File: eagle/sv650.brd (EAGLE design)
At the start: 54.2 x 52 mm, 32 parts, among them Q1 IRLML6344

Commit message: reroute some traces to be cleaner ordered v4.6 via oshpark
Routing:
- net GND: track 161.4 -> 159.8 mm
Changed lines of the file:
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@@
 </element>
 <element name="JP3" library="jumper" package="JP2" value="" x="18.29" y="44.29" smashed="yes" rot="MR90">
-<attribute name="NAME" x="16.401" y="49.574" size="1.27" layer="26" ratio="10" rot="MR180"/>
+<attribute name="NAME" x="14.201" y="43.004" size="1.27" layer="26" ratio="10" rot="MR90"/>
 <attribute name="VALUE" x="13.972" y="40.734" size="1.27" layer="28" ratio="10" rot="MR90"/>
 </element>
@@
 <wire x1="9.1152" y1="16.128" x2="9.1152" y2="11.7152" width="0.3048" layer="1"/>
 <wire x1="9.1152" y1="11.7152" x2="8.38" y2="10.98" width="0.3048" layer="1"/>
-<wire x1="8.38" y1="10.98" x2="7.16" y2="10.98" width="0.3048" layer="1"/>
-<wire x1="7.16" y1="10.98" x2="6.1" y2="10.98" width="0.3048" layer="1"/>
-<wire x1="6.1" y1="10.98" x2="4.37" y2="12.71" width="0.3048" layer="1"/>
-<wire x1="4.37" y1="12.71" x2="4.37" y2="14.57" width="0.3048" layer="1"/>
-<wire x1="4.37" y1="14.57" x2="4.29" y2="14.65" width="0.3048" layer="1"/>
-<wire x1="7.16" y1="10.98" x2="7.16" y2="8.36" width="0.3048" layer="1"/>
+<wire x1="8.38" y1="10.98" x2="7.16" y2="9.85" width="0.3048" layer="1"/>
+<wire x1="7.16" y1="9.85" x2="7.16" y2="8.36" width="0.3048" layer="1"/>
 <wire x1="17.12" y1="19.61" x2="17.17" y2="19.61" width="0.3048" layer="16"/>
 <wire x1="17.17" y1="19.61" x2="17.17" y2="22.56" width="0.3048" layer="16"/>
@@
 <wire x1="4.75" y1="6.57" x2="4.75" y2="5.84" width="0.3048" layer="1"/>
 <wire x1="4.75" y1="5.84" x2="3.62" y2="4.71" width="0.3048" layer="1"/>
-<wire x1="5.12" y1="9.86" x2="5.66" y2="9.86" width="0.3048" layer="1"/>
-<wire x1="5.66" y1="9.86" x2="7.16" y2="8.36" width="0.3048" layer="1"/>
 <wire x1="16.36" y1="14.36" x2="16.36" y2="15.15" width="0.3048" layer="1"/>
 <wire x1="16.36" y1="15.15" x2="18.32" y2="17.11" width="0.3048" layer="1"/>
@@
 <wire x1="19.34" y1="43.26" x2="10.04" y2="43.26" width="0.3048" layer="1"/>
 <wire x1="10.04" y1="43.26" x2="9.275784375" y2="42.495784375" width="0.3048" layer="16"/>
+<wire x1="4.29" y1="14.65" x2="5.12" y2="13.82" width="0.3048" layer="1"/>
+<wire x1="5.12" y1="13.82" x2="5.12" y2="9.86" width="0.3048" layer="1"/>
+<wire x1="5.12" y1="9.86" x2="6.17" y2="9.85" width="0.3048" layer="1"/>
+<wire x1="6.17" y1="9.85" x2="7.16" y2="9.85" width="0.3048" layer="1"/>
 </signal>
 <signal name="N$2">

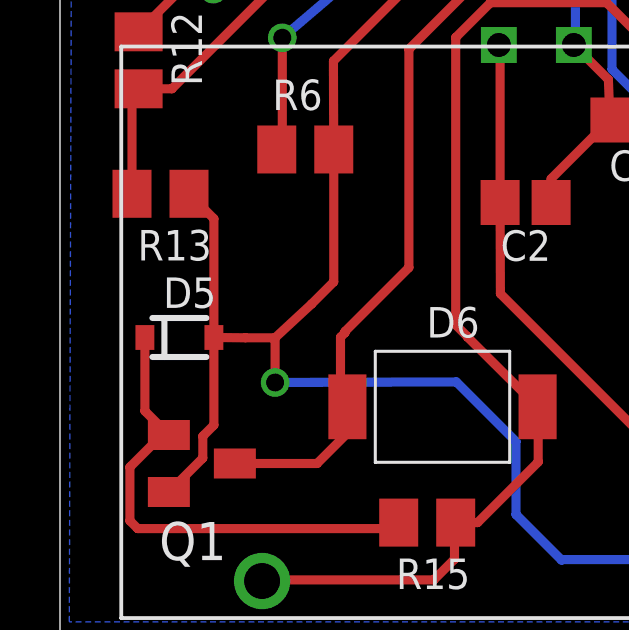
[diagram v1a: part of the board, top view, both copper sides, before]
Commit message: switch D5 to a SOD-123 package
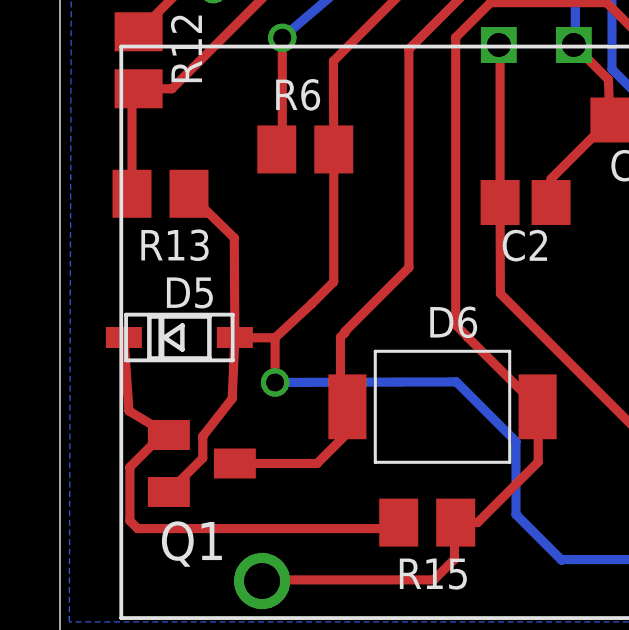
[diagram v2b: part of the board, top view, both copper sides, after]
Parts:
- D5: device SparkFun-DiscreteSemi:SOD-323 -> adafruit:SOD-123
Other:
- board text added: "20140907"
- board text added: "http://synfin.net/sv650ecu SV650 ECU Decoder v4.7"
- board text removed: "20140518"
- board text removed: "http://synfin.net/sv650ecu SV650 ECU Decoder v4.6"
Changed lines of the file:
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@@
 <?xml version="1.0" encoding="utf-8"?>
 <!DOCTYPE eagle SYSTEM "eagle.dtd">
-<eagle version="6.5.0">
+<eagle version="7.1.0">
 <drawing>
 <settings>
@@
 <hole x="50.546" y="29.464" drill="5.1562"/>
 <text x="40.548" y="48.252" size="1.27" layer="22" font="vector" rot="MR0">http://synfin.net/sv650ecu
-SV650 ECU Decoder v4.6</text>
+SV650 ECU Decoder v4.7</text>
 <text x="53.534" y="36.688" size="1.27" layer="22" rot="MR270">S/N:</text>
 <text x="8.906" y="50.432" size="1.27" layer="112">EFI</text>
@@
 <text x="41.712" y="50.402" size="1.27" layer="112">NTRL</text>
 <text x="41.3964" y="37.2906" size="1.27" layer="112">Fuel</text>
-<text x="40.624" y="46.558" size="1.016" layer="22" rot="MR0">20140518</text>
+<text x="40.624" y="46.558" size="1.016" layer="22" rot="MR0">20140907</text>
 <rectangle x1="45.638" y1="32.582" x2="51.734" y2="51.568" layer="22"/>
 <text x="5.75" y="33.8" size="1.27" layer="25">Mode</text>
@@
 <pass name="Default">
 <param name="RoutingGrid" value="50mil"/>
+<param name="AutoGrid" value="1"/>
+<param name="Efforts" value="0"/>
+<param name="TopRouterVariant" value="1"/>
 <param name="tpViaShape" value="round"/>
 <param name="PrefDir.1" value="|"/>
@@
 <attribute name="NAME" x="11.194" y="1.476" size="1.016" layer="25"/>
 </element>
-<element name="D5" library="SparkFun-DiscreteSemi" package="SOD-323" value="10V Z" x="3.97" y="9.86" smashed="yes">
+<element name="D5" library="adafruit" package="SOD-123" value="10V Z" x="3.97" y="9.86" smashed="yes">
 <attribute name="NAME" x="3.431" y="10.846" size="1.016" layer="25"/>
 </element>
@@
 </polygon>
 <contactref element="D5" pad="A"/>
-<wire x1="5.12" y1="9.86" x2="5.12" y2="6.94" width="0.3048" layer="1"/>
+<wire x1="5.82" y1="9.86" x2="5.73" y2="7.82" width="0.3048" layer="1"/>
 <contactref element="Q1" pad="2"/>
-<wire x1="5.12" y1="6.94" x2="4.75" y2="6.57" width="0.3048" layer="1"/>
+<wire x1="5.73" y1="7.82" x2="4.75" y2="6.57" width="0.3048" layer="1"/>
 <wire x1="4.75" y1="6.57" x2="4.75" y2="5.84" width="0.3048" layer="1"/>
 <wire x1="4.75" y1="5.84" x2="3.62" y2="4.71" width="0.3048" layer="1"/>
@@
 <wire x1="19.34" y1="43.26" x2="10.04" y2="43.26" width="0.3048" layer="1"/>
 <wire x1="10.04" y1="43.26" x2="9.275784375" y2="42.495784375" width="0.3048" layer="16"/>
-<wire x1="4.29" y1="14.65" x2="5.12" y2="13.82" width="0.3048" layer="1"/>
-<wire x1="5.12" y1="13.82" x2="5.12" y2="9.86" width="0.3048" layer="1"/>
-<wire x1="5.12" y1="9.86" x2="6.17" y2="9.85" width="0.3048" layer="1"/>
+<wire x1="4.29" y1="14.65" x2="5.8" y2="13.18" width="0.3048" layer="1"/>
+<wire x1="5.8" y1="13.18" x2="5.82" y2="9.86" width="0.3048" layer="1"/>
+<wire x1="5.82" y1="9.86" x2="6.17" y2="9.85" width="0.3048" layer="1"/>
 <wire x1="6.17" y1="9.85" x2="7.16" y2="9.85" width="0.3048" layer="1"/>
 </signal>
@@
 <contactref element="R15" pad="1"/>
 <contactref element="D5" pad="C"/>
-<wire x1="2.82" y1="9.86" x2="2.82" y2="7.41" width="0.3048" layer="1"/>
-<wire x1="2.82" y1="7.41" x2="3.62" y2="6.61" width="0.3048" layer="1"/>
+<wire x1="2.12" y1="9.86" x2="2.29" y2="7.41" width="0.3048" layer="1"/>
+<wire x1="2.29" y1="7.41" x2="3.62" y2="6.61" width="0.3048" layer="1"/>
 <wire x1="3.62" y1="6.61" x2="3.39" y2="6.61" width="0.3048" layer="1"/>
 <wire x1="3.39" y1="6.61" x2="2.32" y2="5.54" width="0.3048" layer="1"/>

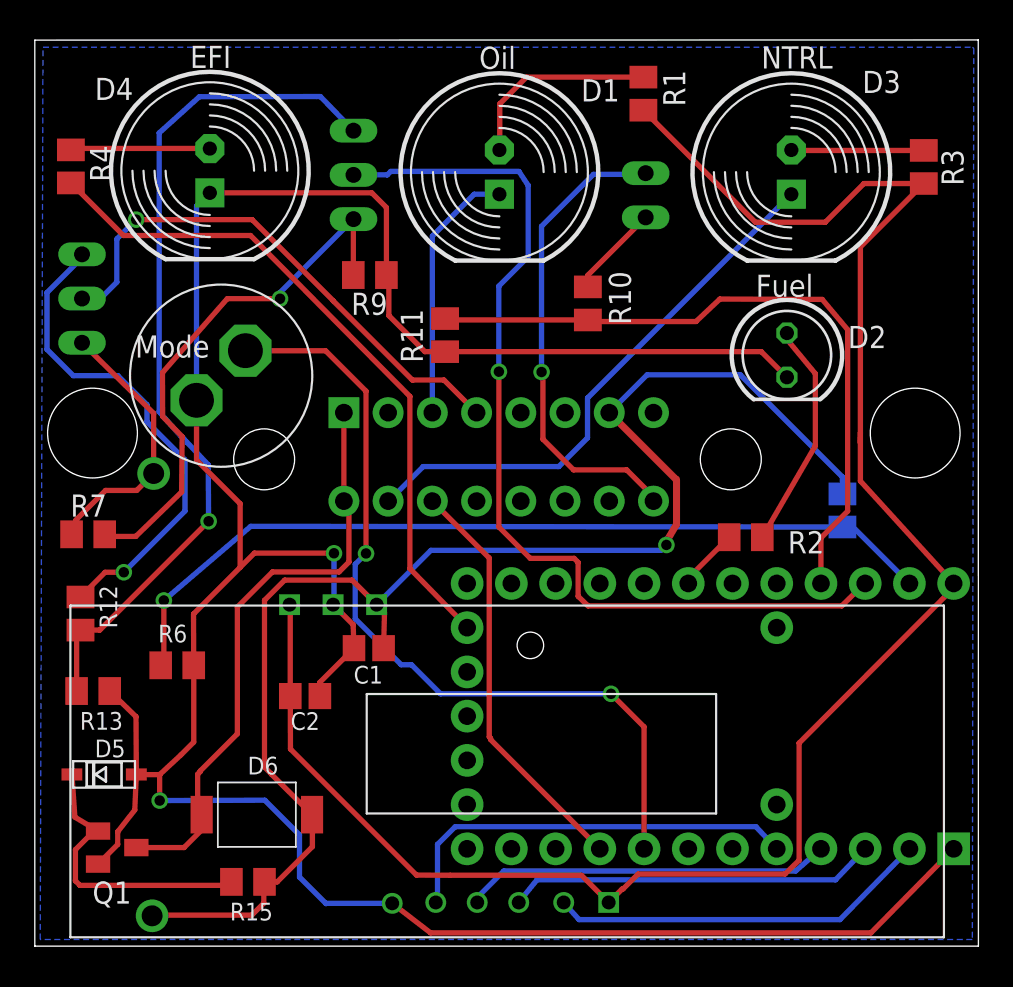
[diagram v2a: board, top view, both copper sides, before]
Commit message: First pass at using Nokia LCD display
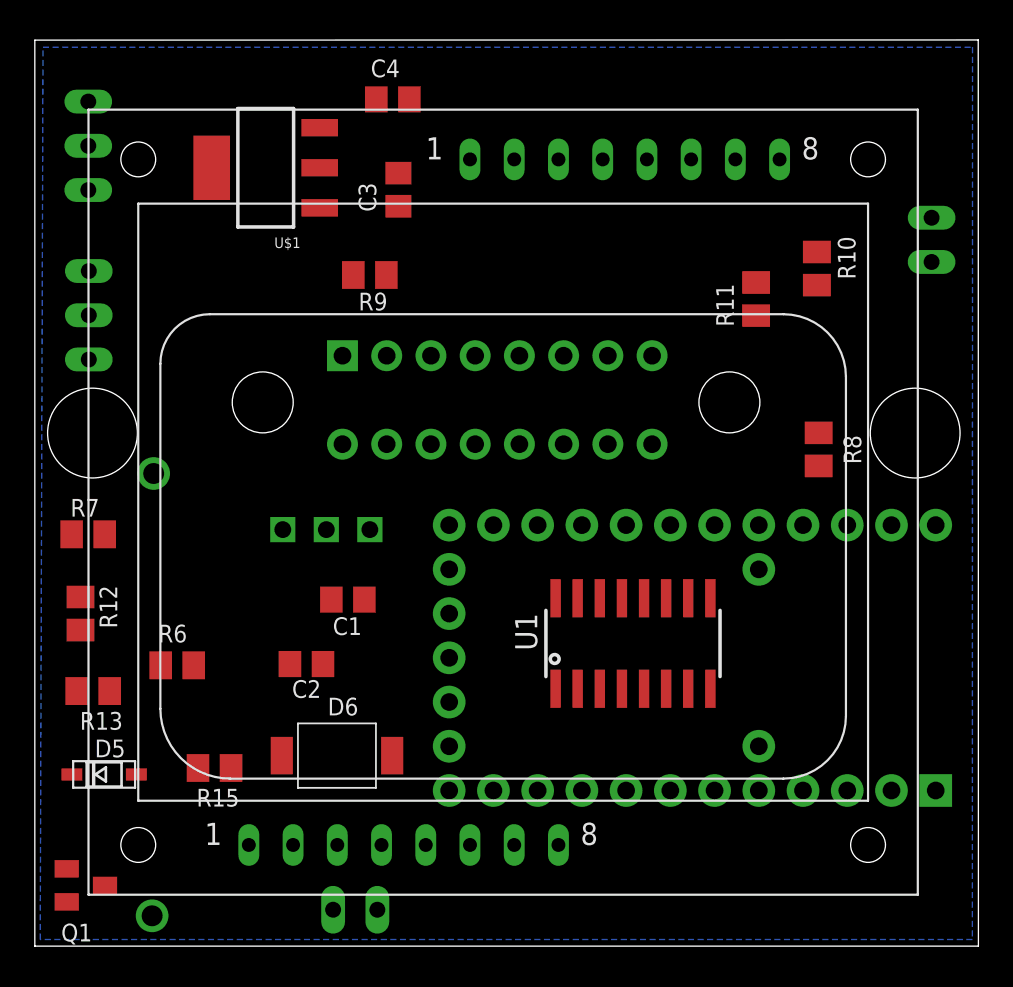
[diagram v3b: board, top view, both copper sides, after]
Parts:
- removed D1: Red, led:LED10MM
- removed D2: Blue, led:LED5MM
- removed D3: Green, led:LED10MM
- removed D4: Yellow, led:LED10MM
- removed R1: 160, resistor:M0805
- removed R2, R3, R4: 150, resistor:M0805
- removed U$10: R13-509A-05-BB/R13-509A-05-BR, synfinatic:R13-509A-05-BB/R13-509A-05-BR
- removed U$5: (no value), synfinatic:STANDOFF
- added C3: 4.7uF, resistor:C0805
- added C4: 1uF, resistor:C0805
- added JP4: enable-backlight, jumper:JP1
- added LCD1: INEX-PCD8544BOTTOM-CONNECTED, synfinatic:INEX-PCD8544-TOP-BOTTOM
- added U1: 74HC4050D, microbuilder:SOIC16
- JP1: value (none) -> enable-very-low-fuel
- JP2: value (none) -> fuel-select1
- JP3: value (none) -> fuel-select2
- U$1: value OASIS-7-SEG-DISPLAY -> MCP1825SOT-223-3; device synfinatic:OASIS-7-SEG-DISPLAY -> synfinatic:SOT-223
- moved U$1 45.6 mm to (13.2, 44.7), turned to 90 degrees
- moved R11 18.0 mm to (41.4, 37.2)
- moved JP1 16.6 mm to (51.5, 40.6)
- moved JP3 15.3 mm to (3.06, 46.0)
- moved R10 13.3 mm to (44.9, 38.9)
- moved R15 6.82 mm to (10.3, 10.2)
- moved D6 5.71 mm to (17.3, 10.9)
- moved U$2 4.33 mm to (11.5, 25.3)
- moved R8 3.76 mm to (45.0, 28.5), flipped to the top
- moved $U3 3.50 mm to (37.8, 16.6)
- moved U$3 3.27 mm to (38.5, 25.9)
- moved C1 3.04 mm to (18.0, 19.9)
- moved Q1 2.82 mm to (2.92, 3.49)
- moved C2 1.84 mm to (15.6, 16.2)
- moved JP2 1.04 mm to (3.09, 36.2)
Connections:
- removed net MODE: $U3.D1, U$10.P$2
- removed net N$3: $U3.B1, U$1.P$3
- removed net N$4: $U3.B2, U$1.P$4
- removed net N$5: $U3.B3, U$1.P$5
- removed net N$6: D3.A, R3.1
- removed net N$7: D2.A, R2.1
- removed net R2: D4.A, R4.1
- new net 3.3V: C4.1, JP4.1, LCD1.P$1, U$1.3, U1.1
- new net CLK: $U3.B1, U1.11
- new net D/C: $U3.B3, U1.7
- new net MOSI: $U3.B2, U1.9
- new net N$13: LCD1.P$5, U1.6
- new net N$15: LCD1.P$6, U1.10
- new net RST: $U3.B4, U1.5
- new net SCE: $U3.B0, U1.3
- net 5V: now also C3.1, U$1.1; no longer R1.2, R3.2, U$1.P$1
- net GND: now also C3.2, C4.2, LCD1.P$2, U$1.2, U$1.4, U1.8; no longer D2.K, D4.K, U$1.P$6, U$10.P$1
- net N$16: now also LCD1.P$7, U1.12; no longer $U3.F7, R2.2
- net N$2: now also JP4.2, LCD1.P$8; no longer $U3.B0, U$1.P$2
- net N$8: now also LCD1.P$3, U1.2; no longer D1.A, R1.1
- net N$9: now also LCD1.P$4, U1.4; no longer $U3.D4, R4.2
- net NTRL: now also $U3.D3; no longer D3.K
- net OIL: now also $U3.D4; no longer D1.K
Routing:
- net GND: track 159.5 -> 0.00 mm, vias 2 -> 0
- net 5V: track 108.5 -> 0.00 mm
- net +12V: track 82.1 -> 0.00 mm, vias 1 -> 0
- net FUEL_ADC: track 55.4 -> 0.00 mm, vias 1 -> 0
- net FUEL_B_ADC: track 50.3 -> 0.00 mm, vias 1 -> 0
- net BATTMON: track 49.5 -> 0.00 mm, vias 1 -> 0
- net MODE: track 47.4 -> 0.00 mm, vias 2 -> 0
- net FUEL2_ADC: track 39.7 -> 0.00 mm
- net N$9: track 39.2 -> 0.00 mm
- net GND_MAIN: track 34.2 -> 0.00 mm
- net NTRL: track 31.8 -> 0.00 mm
- net FUEL_A_ADC: track 31.1 -> 0.00 mm, vias 1 -> 0
- net N$12: track 30.6 -> 0.00 mm, vias 1 -> 0
- net FUEL_B: track 28.3 -> 0.00 mm, vias 1 -> 0
- net N$14: track 27.5 -> 0.00 mm, vias 1 -> 0
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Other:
- board text added: "20150328"
- board text added: "Backlght"
- board text added: "http://synfin.net/sv650ecu SV650 ECU Decoder v5.0"
- board text removed: "20140907"
- board text removed: "EFI"
- board text removed: "Fuel"
- board text removed: "Mode"
- board text removed: "NTRL"
- board text removed: "Oil"
- board text removed: "http://synfin.net/sv650ecu SV650 ECU Decoder v4.7"

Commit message: update board to have a 6mm switch on front
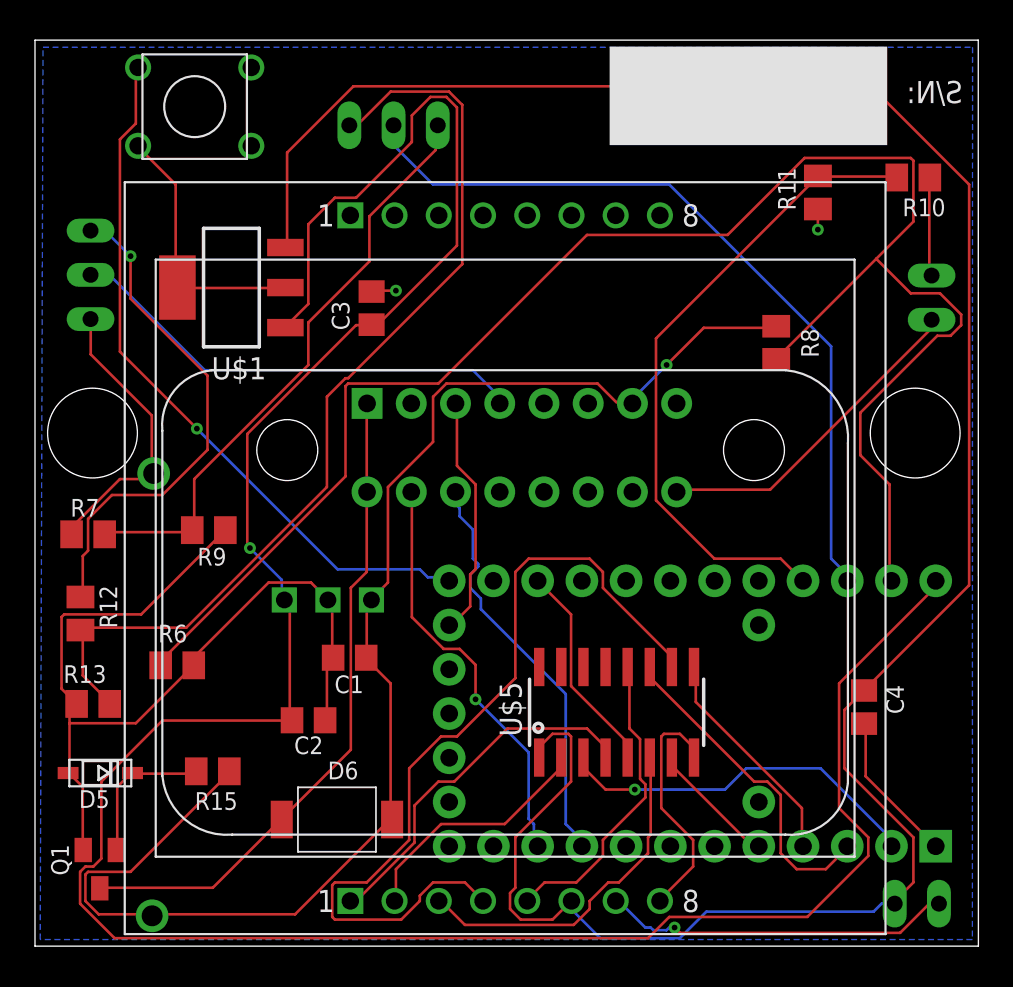
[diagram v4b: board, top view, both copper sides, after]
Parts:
- removed U1: 74HC4050D, microbuilder:SOIC16
- added S1: Mode, synfinatic:ADTS6**V
- added U$5: 74HC4050D, microbuilder:SOIC16
- LCD1: value INEX-PCD8544BOTTOM-CONNECTED -> INEX-PCD8544NOKIA-5110-EBAY-NOHOLES-BOTTOM; device synfinatic:INEX-PCD8544-TOP-BOTTOM -> synfinatic:NOKIA-5110-EBAY-NOHOLES
- moved C4 44.2 mm to (47.6, 13.7), turned to 270 degrees
- moved JP4 32.3 mm to (50.6, 2.44)
- moved JP3 17.6 mm to (20.6, 47.1), turned to 0 degrees
- moved R9 17.3 mm to (9.98, 23.9)
- moved R10 7.62 mm to (50.4, 44.1), turned to 180 degrees
- moved U$1 7.16 mm to (11.3, 37.8)
- moved R11 7.08 mm to (45.0, 43.3)
- moved C3 6.97 mm to (19.3, 36.6)
- moved R8 6.59 mm to (42.6, 34.6)
- moved U$2 4.04 mm to (11.6, 21.2)
- moved LCD1 3.89 mm to (27.0, 18.5)
- moved D6 3.67 mm to (17.3, 7.27)
- moved C1 3.34 mm to (18.1, 16.6)
- moved JP1 3.32 mm to (51.5, 37.2), turned to 0 degrees
- moved C2 3.23 mm to (15.7, 13.0)
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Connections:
- new net N$3: $U3.D6, S1.P$2
- net 3.3V: now also LCD1.P$6, U$5.1; no longer LCD1.P$1, U1.1
- net CLK: now also U$5.11; no longer U1.11
- net D/C: now also U$5.7; no longer U1.7
- net GND: now also LCD1.P$8, S1.P$1, U$5.8; no longer LCD1.P$2, U1.8
- net MOSI: now also U$5.9; no longer U1.9
- net N$13: now also LCD1.P$3, U$5.6; no longer LCD1.P$5, U1.6
- net N$15: now also LCD1.P$4, U$5.10; no longer LCD1.P$6, U1.10
- net N$16: now also LCD1.P$5, U$5.12; no longer LCD1.P$7, U1.12
- net N$2: now also LCD1.P$7; no longer LCD1.P$8
- net N$8: now also LCD1.P$2, U$5.2; no longer LCD1.P$3, U1.2
- net N$9: now also LCD1.P$1, U$5.4; no longer LCD1.P$4, U1.4
- net RST: now also U$5.5; no longer U1.5
- net SCE: now also U$5.3; no longer U1.3
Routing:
- net 5V: track 0.00 -> 148.2 mm, vias 0 -> 1
- net 3.3V: track 0.00 -> 133.9 mm
- net BATTMON: track 0.00 -> 98.3 mm
- net GND: track 0.00 -> 92.3 mm, vias 0 -> 2
- net +12V: track 0.00 -> 81.5 mm, vias 0 -> 1
- net FUEL_B_ADC: track 0.00 -> 55.4 mm
- net N$15: track 0.00 -> 48.8 mm
- net FUEL_ADC: track 0.00 -> 44.9 mm
- net N$3: track 0.00 -> 41.2 mm, vias 0 -> 1
- net GND_MAIN: track 0.00 -> 38.0 mm
- net FUEL2_ADC: track 0.00 -> 37.4 mm
- net FUEL_A_ADC: track 0.00 -> 34.3 mm
- net FUEL_B: track 0.00 -> 29.1 mm, vias 0 -> 1
- net N$12: track 0.00 -> 26.8 mm
- net NTRL: track 0.00 -> 23.9 mm, vias 0 -> 1
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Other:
- board text added: "20150423"
- board text removed: "20150328"
